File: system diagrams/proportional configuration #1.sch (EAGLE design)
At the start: 15 parts

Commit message: small mechanical changes to some cards, output connectors were moved around
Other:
- note added: "Air Input Valve"
- note added: "Oxygen Input Valve"
- note added: "Patient Inflating Valve"
- note added: "Respiration Valve (Proportional)"
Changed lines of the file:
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@@
 <wire x1="-135.89" y1="-15.24" x2="-134.62" y2="-15.24" width="0.2286" layer="94"/>
 <wire x1="-135.89" y1="-15.24" x2="-128.27" y2="-20.32" width="0.2286" layer="94"/>
+<text x="-147.32" y="-29.21" size="2.54" layer="94">Patient Inflating Valve</text>
+<text x="-152.4" y="-8.89" size="2.54" layer="94">Respiration Valve (Proportional)</text>
+<text x="-144.78" y="11.43" size="2.54" layer="94">Oxygen Input Valve</text>
+<text x="-139.7" y="31.75" size="2.54" layer="94">Air Input Valve</text>
 </plain>
 <instances>

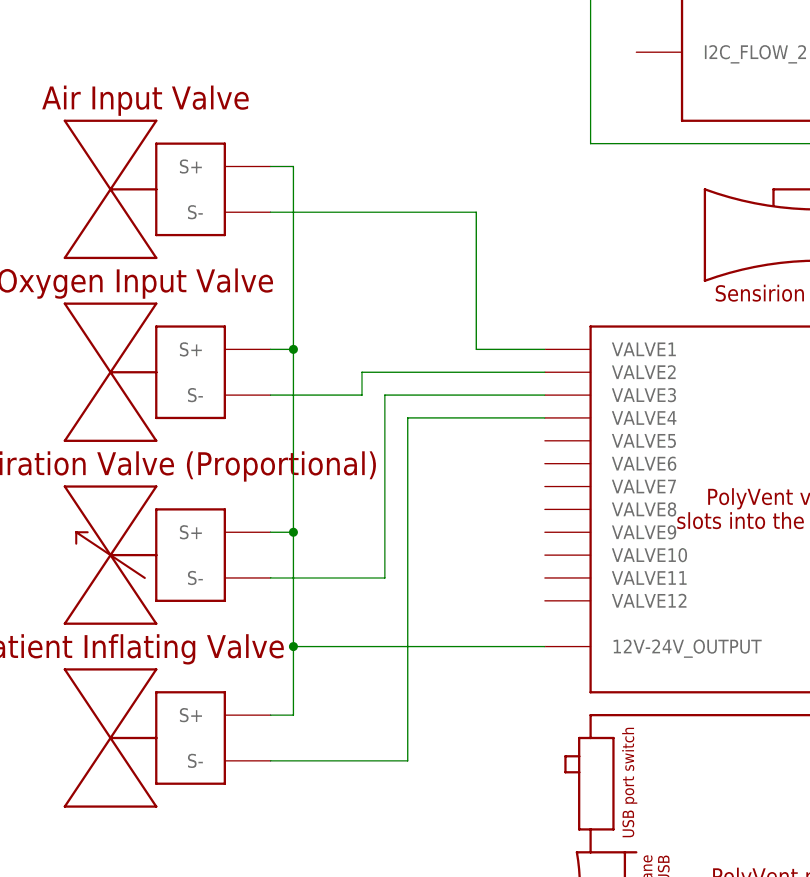
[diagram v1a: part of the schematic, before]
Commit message: added diode for proportional valve
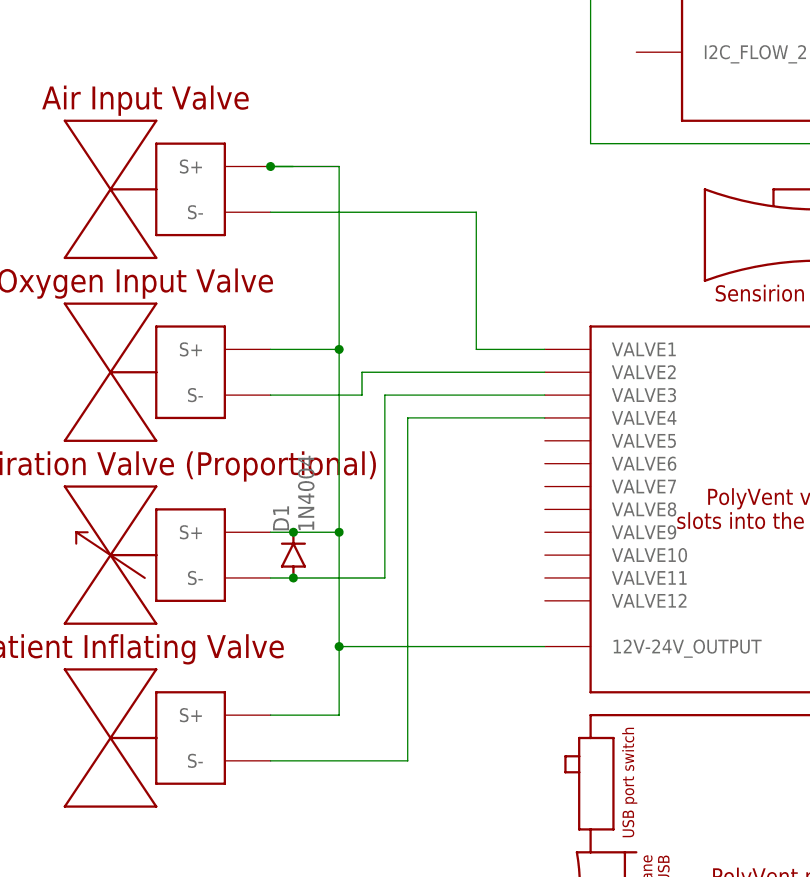
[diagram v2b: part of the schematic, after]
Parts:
- added D1: 1N4004, diode:1N4004
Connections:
- net N$12: now also D1.A
- net N$9: now also D1.C
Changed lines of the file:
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@@
 <part name="U$21" library="polyvent card schematics" deviceset="SOLENOID_VALVE" device=""/>
 <part name="U$22" library="polyvent card schematics" deviceset="OXYGEN_SENSOR" device=""/>
+<part name="D1" library="diode" library_urn="urn:adsk.eagle:library:210" deviceset="1N4004" device="" package3d_urn="urn:adsk.eagle:package:43336/1"/>
 </parts>
 <sheets>
@@
 <instance part="U$21" gate="G$1" x="-132.08" y="-38.1" smashed="yes" rot="R270"/>
 <instance part="U$22" gate="G$1" x="-86.36" y="53.34" smashed="yes" rot="R180"/>
+<instance part="D1" gate="1" x="-111.76" y="-17.78" smashed="yes" rot="R90">
+<attribute name="NAME" x="-112.2426" y="-15.24" size="1.778" layer="95" rot="R90"/>
+<attribute name="VALUE" x="-109.4486" y="-15.24" size="1.778" layer="96" rot="R90"/>
+</instance>
 </instances>
 <busses>
@@
 <segment>
 <pinref part="U$21" gate="G$1" pin="S+"/>
-<wire x1="-114.3" y1="-35.56" x2="-111.76" y2="-35.56" width="0.1524" layer="91"/>
-<wire x1="-111.76" y1="-35.56" x2="-111.76" y2="-27.94" width="0.1524" layer="91"/>
-<pinref part="U$11" gate="G$1" pin="S+"/>
-<wire x1="-111.76" y1="-27.94" x2="-111.76" y2="-15.24" width="0.1524" layer="91"/>
-<wire x1="-111.76" y1="-15.24" x2="-111.76" y2="5.08" width="0.1524" layer="91"/>
-<wire x1="-111.76" y1="5.08" x2="-111.76" y2="25.4" width="0.1524" layer="91"/>
-<wire x1="-111.76" y1="25.4" x2="-114.3" y2="25.4" width="0.1524" layer="91"/>
+<wire x1="-114.3" y1="-35.56" x2="-106.68" y2="-35.56" width="0.1524" layer="91"/>
+<wire x1="-106.68" y1="-35.56" x2="-106.68" y2="-27.94" width="0.1524" layer="91"/>
+<wire x1="-106.68" y1="-27.94" x2="-106.68" y2="-15.24" width="0.1524" layer="91"/>
+<wire x1="-106.68" y1="-15.24" x2="-106.68" y2="5.08" width="0.1524" layer="91"/>
 <pinref part="U$16" gate="G$1" pin="S+"/>
-<wire x1="-114.3" y1="5.08" x2="-111.76" y2="5.08" width="0.1524" layer="91"/>
-<junction x="-111.76" y="5.08"/>
+<wire x1="-114.3" y1="5.08" x2="-106.68" y2="5.08" width="0.1524" layer="91"/>
 <pinref part="U$17" gate="G$1" pin="S+"/>
 <wire x1="-114.3" y1="-15.24" x2="-111.76" y2="-15.24" width="0.1524" layer="91"/>
+<junction x="-106.68" y="-15.24"/>
+<pinref part="U$8" gate="G$1" pin="12V-24V_OUTPUT"/>
+<wire x1="-111.76" y1="-15.24" x2="-106.68" y2="-15.24" width="0.1524" layer="91"/>
+<wire x1="-106.68" y1="-27.94" x2="-83.82" y2="-27.94" width="0.1524" layer="91"/>
+<junction x="-106.68" y="-27.94"/>
+<pinref part="U$11" gate="G$1" pin="S+"/>
+<wire x1="-111.76" y1="25.4" x2="-114.3" y2="25.4" width="0.1524" layer="91"/>
+<wire x1="-106.68" y1="5.08" x2="-106.68" y2="25.4" width="0.1524" layer="91"/>
+<wire x1="-106.68" y1="25.4" x2="-114.3" y2="25.4" width="0.1524" layer="91"/>
+<junction x="-106.68" y="5.08"/>
+<junction x="-114.3" y="25.4"/>
+<pinref part="D1" gate="1" pin="C"/>
 <junction x="-111.76" y="-15.24"/>
-<pinref part="U$8" gate="G$1" pin="12V-24V_OUTPUT"/>
-<wire x1="-111.76" y1="-27.94" x2="-83.82" y2="-27.94" width="0.1524" layer="91"/>
-<junction x="-111.76" y="-27.94"/>
 </segment>
 </net>
@@
 <segment>
 <pinref part="U$17" gate="G$1" pin="S-"/>
-<wire x1="-114.3" y1="-20.32" x2="-101.6" y2="-20.32" width="0.1524" layer="91"/>
+<wire x1="-114.3" y1="-20.32" x2="-111.76" y2="-20.32" width="0.1524" layer="91"/>
+<wire x1="-111.76" y1="-20.32" x2="-101.6" y2="-20.32" width="0.1524" layer="91"/>
 <wire x1="-101.6" y1="-20.32" x2="-101.6" y2="0" width="0.1524" layer="91"/>
 <pinref part="U$8" gate="G$1" pin="VALVE3"/>
 <wire x1="-101.6" y1="0" x2="-83.82" y2="0" width="0.1524" layer="91"/>
+<pinref part="D1" gate="1" pin="A"/>
+<junction x="-111.76" y="-20.32"/>
 </segment>
 </net>
@@
 which will not be processed correctly with this version.
 </note>
+<note version="8.2" severity="warning">
+Since Version 8.2, EAGLE supports online libraries. The ids
+of those online libraries will not be understood (or retained)
+with this version.
+</note>
+<note version="8.3" severity="warning">
+Since Version 8.3, EAGLE supports URNs for individual library
+assets (packages, symbols, and devices). The URNs of those assets
+will not be understood (or retained) with this version.
+</note>
+<note version="8.3" severity="warning">
+Since Version 8.3, EAGLE supports the association of 3D packages
+with devices in libraries, schematics, and board files. Those 3D
+packages will not be understood (or retained) with this version.
+</note>
 </compatibility>
